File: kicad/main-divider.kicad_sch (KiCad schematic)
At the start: 28 parts, among them U11 TL074, U12 CD4024

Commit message: component positioning mostly done
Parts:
- C46, C47, C48: footprint rumblesan-standard-parts:C_Rect_L7.0mm_W3.5mm_P5.00mm -> rumblesan-standard-parts:C_Rect_L7.0mm_W2.5mm_P5.00mm
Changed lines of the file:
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@@
       (effects (font (size 1.27 1.27)) (justify left))
     )
-    (property "Footprint" "rumblesan-standard-parts:C_Rect_L7.0mm_W3.5mm_P5.00mm" (id 2) (at 248.285 44.45 90)
+    (property "Footprint" "rumblesan-standard-parts:C_Rect_L7.0mm_W2.5mm_P5.00mm" (id 2) (at 248.285 44.45 90)
       (effects (font (size 1.27 1.27)) hide)
     )
@@
       (effects (font (size 1.27 1.27)) (justify left))
     )
-    (property "Footprint" "rumblesan-standard-parts:C_Rect_L7.0mm_W3.5mm_P5.00mm" (id 2) (at 117.475 49.53 90)
+    (property "Footprint" "rumblesan-standard-parts:C_Rect_L7.0mm_W2.5mm_P5.00mm" (id 2) (at 117.475 49.53 90)
       (effects (font (size 1.27 1.27)) hide)
     )
@@
       (effects (font (size 1.27 1.27)) (justify left))
     )
-    (property "Footprint" "rumblesan-standard-parts:C_Rect_L7.0mm_W3.5mm_P5.00mm" (id 2) (at 248.285 57.15 90)
-      (effects (font (size 1.27 1.27)) hide)
-    )
+    (property "Footprint" "rumblesan-standard-parts:C_Rect_L7.0mm_W2.5mm_P5.00mm" (id 2) (at 248.285 57.15 90)
+      (effects (font (size 1.27 1.27)) hide)
+    )

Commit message: initial layout done
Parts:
- removed R65: 47k, rumblesan-standard-parts:R_Axial_DIN0207_L6.3mm_D2.5mm_P10.16mm_Horizontal, symbol rumblesan-standard-parts:R
- C45: footprint rumblesan-standard-parts:C_Rect_L7.0mm_W3.5mm_P5.00mm -> rumblesan-standard-parts:C_Rect_L7.0mm_W2.5mm_P5.00mm
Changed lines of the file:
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@@
   (junction (at 138.43 101.6) (diameter 0) (color 0 0 0 0)
-  )
-  (junction (at 36.83 68.58) (diameter 0) (color 0 0 0 0)
   )
   (junction (at 85.09 68.58) (diameter 0) (color 0 0 0 0)
@@
     (stroke (width 0) (type default) (color 0 0 0 0))
   )
-  (wire (pts (xy 33.02 68.58) (xy 36.83 68.58))
+  (wire (pts (xy 33.02 68.58) (xy 39.37 68.58))
     (stroke (width 0) (type default) (color 0 0 0 0))
   )
@@
     (stroke (width 0) (type default) (color 0 0 0 0))
   )
-  (wire (pts (xy 36.83 68.58) (xy 39.37 68.58))
-    (stroke (width 0) (type default) (color 0 0 0 0))
-  )
   (wire (pts (xy 165.1 83.82) (xy 168.91 83.82))
     (stroke (width 0) (type default) (color 0 0 0 0))
@@
     (stroke (width 0) (type default) (color 0 0 0 0))
   )
-  (wire (pts (xy 36.83 68.58) (xy 36.83 71.12))
-    (stroke (width 0) (type default) (color 0 0 0 0))
-  )
   (wire (pts (xy 168.91 72.39) (xy 156.21 72.39))
     (stroke (width 0) (type default) (color 0 0 0 0))
@@
   )
   (wire (pts (xy 156.21 64.77) (xy 157.48 64.77))
-    (stroke (width 0) (type default) (color 0 0 0 0))
-  )
-  (wire (pts (xy 36.83 78.74) (xy 36.83 81.28))
     (stroke (width 0) (type default) (color 0 0 0 0))
   )
@@
     (pin "2")
   )
-  (symbol (lib_id "power:GND") (at 36.83 81.28 0) (unit 1)
-    (in_bom yes) (on_board yes) (fields_autoplaced)
-    (property "Reference" "#PWR0106" (id 0) (at 36.83 87.63 0)
-      (effects (font (size 1.27 1.27)) hide)
-    )
-    (property "Value" "GND" (id 1) (at 36.83 85.7234 0))
-    (property "Footprint" "" (id 2) (at 36.83 81.28 0)
-      (effects (font (size 1.27 1.27)) hide)
-    )
-    (property "Datasheet" "" (id 3) (at 36.83 81.28 0)
-      (effects (font (size 1.27 1.27)) hide)
-    )
-    (pin "1")
-  )
   (symbol (lib_id "rumblesan-standard-parts:R") (at 161.29 54.61 90) (unit 1)
     (in_bom yes) (on_board yes)
@@
     (property "Reference" "C45" (id 0) (at 54.61 62.7212 90))
     (property "Value" "1nF" (id 1) (at 54.61 65.2581 90))
-    (property "Footprint" "rumblesan-standard-parts:C_Rect_L7.0mm_W3.5mm_P5.00mm" (id 2) (at 53.34 62.865 90)
+    (property "Footprint" "rumblesan-standard-parts:C_Rect_L7.0mm_W2.5mm_P5.00mm" (id 2) (at 53.34 62.865 90)
       (effects (font (size 1.27 1.27)) hide)
     )
@@
     (pin "1")
   )
-  (symbol (lib_id "rumblesan-standard-parts:R") (at 36.83 74.93 0) (unit 1)
-    (in_bom yes) (on_board yes) (fields_autoplaced)
-    (property "Reference" "R65" (id 0) (at 38.608 74.0953 0)
-      (effects (font (size 1.27 1.27)) (justify left))
-    )
-    (property "Value" "47k" (id 1) (at 38.608 76.6322 0)
-      (effects (font (size 1.27 1.27)) (justify left))
-    )
-    (property "Footprint" "rumblesan-standard-parts:R_Axial_DIN0207_L6.3mm_D2.5mm_P10.16mm_Horizontal" (id 2) (at 39.37 77.47 90)
-      (effects (font (size 1.27 1.27)) hide)
-    )
-    (property "Datasheet" "~" (id 3) (at 43.18 74.93 90)
-      (effects (font (size 1.27 1.27)) hide)
-    )
-    (property "Tolerance" "1%" (id 4) (at 41.91 81.28 90)
-      (effects (font (size 1.27 1.27)) hide)
-    )
-    (property "Power" "0.5W" (id 5) (at 41.91 67.31 90)
-      (effects (font (size 1.27 1.27)) hide)
-    )
-    (property "Spec" "metal film" (id 6) (at 41.91 74.93 90)
-      (effects (font (size 1.27 1.27)) hide)
-    )
-    (pin "1")
-    (pin "2")
-  )
   (symbol (lib_id "power:GND") (at 85.09 81.28 0) (unit 1)

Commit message: Final changes for rev01
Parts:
- removed D19: 1n4148, rumblesan-standard-parts:D_DO-35_SOD27_P7.62mm_Horizontal, symbol Device:D
- removed R66, R83: 1k, rumblesan-standard-parts:R_Axial_DIN0207_L6.3mm_D2.5mm_P10.16mm_Horizontal, symbol rumblesan-standard-parts:R
- removed R84: 10k, rumblesan-standard-parts:R_Axial_DIN0207_L6.3mm_D2.5mm_P10.16mm_Horizontal, symbol rumblesan-standard-parts:R
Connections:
- net CLOCK: now also C45.1
- net OUT: now also U11.7, U12.2 (MR)
- net at C45.2: now also R68.1, U11.13 (-)
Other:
- moved on the sheet: C45
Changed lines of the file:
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@@
   (junction (at 233.68 63.5) (diameter 0) (color 0 0 0 0)
-  )
-  (junction (at 208.28 106.68) (diameter 0) (color 0 0 0 0)
   )
   (junction (at 194.31 106.68) (diameter 0) (color 0 0 0 0)
@@
     (stroke (width 0) (type default) (color 0 0 0 0))
   )
-  (wire (pts (xy 208.28 118.11) (xy 208.28 120.65))
-    (stroke (width 0) (type default) (color 0 0 0 0))
-  )
   (wire (pts (xy 85.09 49.53) (xy 91.44 49.53))
     (stroke (width 0) (type default) (color 0 0 0 0))
@@
     (stroke (width 0) (type default) (color 0 0 0 0))
   )
-  (wire (pts (xy 33.02 68.58) (xy 39.37 68.58))
-    (stroke (width 0) (type default) (color 0 0 0 0))
-  )
   (wire (pts (xy 137.16 101.6) (xy 138.43 101.6))
     (stroke (width 0) (type default) (color 0 0 0 0))
   )
-  (wire (pts (xy 194.31 106.68) (xy 196.85 106.68))
+  (wire (pts (xy 194.31 106.68) (xy 199.39 106.68))
     (stroke (width 0) (type default) (color 0 0 0 0))
   )
@@
     (stroke (width 0) (type default) (color 0 0 0 0))
   )
-  (wire (pts (xy 208.28 106.68) (xy 212.09 106.68))
-    (stroke (width 0) (type default) (color 0 0 0 0))
-  )
   (wire (pts (xy 165.1 59.69) (xy 168.91 59.69))
     (stroke (width 0) (type default) (color 0 0 0 0))
   )
-  (wire (pts (xy 58.42 68.58) (xy 62.23 68.58))
+  (wire (pts (xy 80.01 68.58) (xy 85.09 68.58))
     (stroke (width 0) (type default) (color 0 0 0 0))
   )
@@
     (stroke (width 0) (type default) (color 0 0 0 0))
   )
-  (wire (pts (xy 204.47 106.68) (xy 208.28 106.68))
-    (stroke (width 0) (type default) (color 0 0 0 0))
-  )
   (wire (pts (xy 85.09 49.53) (xy 85.09 63.5))
     (stroke (width 0) (type default) (color 0 0 0 0))
   )
-  (wire (pts (xy 69.85 68.58) (xy 85.09 68.58))
-    (stroke (width 0) (type default) (color 0 0 0 0))
-  )
   (wire (pts (xy 156.21 83.82) (xy 157.48 83.82))
     (stroke (width 0) (type default) (color 0 0 0 0))
@@
     (stroke (width 0) (type default) (color 0 0 0 0))
   )
-  (wire (pts (xy 46.99 68.58) (xy 50.8 68.58))
+  (wire (pts (xy 67.31 68.58) (xy 72.39 68.58))
     (stroke (width 0) (type default) (color 0 0 0 0))
   )
@@
   )
   (wire (pts (xy 101.6 69.85) (xy 101.6 124.46))
-    (stroke (width 0) (type default) (color 0 0 0 0))
-  )
-  (wire (pts (xy 208.28 106.68) (xy 208.28 110.49))
     (stroke (width 0) (type default) (color 0 0 0 0))
   )
@@
     (effects (font (size 1.27 1.27)) (justify right))
   )
-  (hierarchical_label "CLOCK" (shape input) (at 33.02 68.58 180)
+  (hierarchical_label "CLOCK" (shape input) (at 67.31 68.58 180)
     (effects (font (size 1.27 1.27)) (justify right))
   )
-  (hierarchical_label "OUT" (shape input) (at 212.09 106.68 0)
+  (hierarchical_label "OUT" (shape input) (at 199.39 106.68 0)
     (effects (font (size 1.27 1.27)) (justify left))
   )
@@
     (pin "1")
   )
-  (symbol (lib_id "rumblesan-standard-parts:C") (at 54.61 68.58 90) (unit 1)
-    (in_bom yes) (on_board yes) (fields_autoplaced)
-    (property "Reference" "C45" (id 0) (at 54.61 62.7212 90))
-    (property "Value" "1nF" (id 1) (at 54.61 65.2581 90))
-    (property "Footprint" "rumblesan-standard-parts:C_Rect_L7.0mm_W2.5mm_P5.00mm" (id 2) (at 53.34 62.865 90)
-      (effects (font (size 1.27 1.27)) hide)
-    )
-    (property "Datasheet" "~" (id 3) (at 54.61 60.96 90)
-      (effects (font (size 1.27 1.27)) hide)
-    )
-    (property "Spec" "ceramic C0G" (id 4) (at 54.61 64.77 90)
-      (effects (font (size 1.27 1.27)) hide)
-    )
-    (property "Tolerance" "5%" (id 5) (at 46.355 64.77 90)
-      (effects (font (size 1.27 1.27)) hide)
-    )
-    (pin "1")
-    (pin "2")
-  )
-  (symbol (lib_id "rumblesan-standard-parts:R") (at 43.18 68.58 90) (unit 1)
-    (in_bom yes) (on_board yes) (fields_autoplaced)
-    (property "Reference" "R66" (id 0) (at 43.18 63.8642 90))
-    (property "Value" "1k" (id 1) (at 43.18 66.4011 90))
-    (property "Footprint" "rumblesan-standard-parts:R_Axial_DIN0207_L6.3mm_D2.5mm_P10.16mm_Horizontal" (id 2) (at 45.72 66.04 90)
-      (effects (font (size 1.27 1.27)) hide)
-    )
-    (property "Datasheet" "~" (id 3) (at 43.18 62.23 90)
-      (effects (font (size 1.27 1.27)) hide)
-    )
-    (property "Tolerance" "1%" (id 4) (at 49.53 63.5 90)
-      (effects (font (size 1.27 1.27)) hide)
-    )
-    (property "Power" "0.5W" (id 5) (at 35.56 63.5 90)
-      (effects (font (size 1.27 1.27)) hide)
-    )
-    (property "Spec" "metal film" (id 6) (at 43.18 63.5 90)
+  (symbol (lib_id "rumblesan-standard-parts:C") (at 76.2 68.58 90) (unit 1)
+    (in_bom yes) (on_board yes) (fields_autoplaced)
+    (property "Reference" "C45" (id 0) (at 76.2 62.7212 90))
+    (property "Value" "1nF" (id 1) (at 76.2 65.2581 90))
+    (property "Footprint" "rumblesan-standard-parts:C_Rect_L7.0mm_W2.5mm_P5.00mm" (id 2) (at 74.93 62.865 90)
+      (effects (font (size 1.27 1.27)) hide)
+    )
+    (property "Datasheet" "~" (id 3) (at 76.2 60.96 90)
+      (effects (font (size 1.27 1.27)) hide)
+    )
+    (property "Spec" "ceramic C0G" (id 4) (at 76.2 64.77 90)
+      (effects (font (size 1.27 1.27)) hide)
+    )
+    (property "Tolerance" "5%" (id 5) (at 67.945 64.77 90)
       (effects (font (size 1.27 1.27)) hide)
     )
@@
     (pin "2")
   )
-  (symbol (lib_id "rumblesan-standard-parts:R") (at 208.28 114.3 0) (unit 1)
-    (in_bom yes) (on_board yes) (fields_autoplaced)
-    (property "Reference" "R84" (id 0) (at 210.058 113.4653 0)
-      (effects (font (size 1.27 1.27)) (justify left))
-    )
-    (property "Value" "10k" (id 1) (at 210.058 116.0022 0)
-      (effects (font (size 1.27 1.27)) (justify left))
-    )
-    (property "Footprint" "rumblesan-standard-parts:R_Axial_DIN0207_L6.3mm_D2.5mm_P10.16mm_Horizontal" (id 2) (at 210.82 116.84 90)
-      (effects (font (size 1.27 1.27)) hide)
-    )
-    (property "Datasheet" "~" (id 3) (at 214.63 114.3 90)
-      (effects (font (size 1.27 1.27)) hide)
-    )
-    (property "Tolerance" "1%" (id 4) (at 213.36 120.65 90)
-      (effects (font (size 1.27 1.27)) hide)
-    )
-    (property "Power" "0.5W" (id 5) (at 213.36 106.68 90)
-      (effects (font (size 1.27 1.27)) hide)
-    )
-    (property "Spec" "metal film" (id 6) (at 213.36 114.3 90)
-      (effects (font (size 1.27 1.27)) hide)
-    )
-    (pin "1")
-    (pin "2")
-  )
   (symbol (lib_id "power:VCC") (at 124.46 40.64 0) (unit 1)
     (in_bom yes) (on_board yes) (fields_autoplaced)
@@
     )
     (property "Spec" "metal film" (id 6) (at 149.86 54.61 90)
-      (effects (font (size 1.27 1.27)) hide)
-    )
-    (pin "1")
-    (pin "2")
-  )
-  (symbol (lib_id "Device:D") (at 66.04 68.58 180) (unit 1)
-    (in_bom yes) (on_board yes) (fields_autoplaced)
-    (property "Reference" "D19" (id 0) (at 66.04 63.6102 0))
-    (property "Value" "1n4148" (id 1) (at 66.04 66.1471 0))
-    (property "Footprint" "rumblesan-standard-parts:D_DO-35_SOD27_P7.62mm_Horizontal" (id 2) (at 66.04 68.58 0)
-      (effects (font (size 1.27 1.27)) hide)
-    )
-    (property "Datasheet" "~" (id 3) (at 66.04 68.58 0)
       (effects (font (size 1.27 1.27)) hide)
     )
@@
     (pin "2")
   )
-  (symbol (lib_id "power:GND") (at 208.28 120.65 0) (unit 1)
-    (in_bom yes) (on_board yes) (fields_autoplaced)
-    (property "Reference" "#PWR0116" (id 0) (at 208.28 127 0)
-      (effects (font (size 1.27 1.27)) hide)
-    )
-    (property "Value" "GND" (id 1) (at 208.28 125.0934 0))
-    (property "Footprint" "" (id 2) (at 208.28 120.65 0)
-      (effects (font (size 1.27 1.27)) hide)
-    )
-    (property "Datasheet" "" (id 3) (at 208.28 120.65 0)
-      (effects (font (size 1.27 1.27)) hide)
-    )
-    (pin "1")
-  )
   (symbol (lib_id "rumblesan-standard-parts:R") (at 161.29 83.82 270) (unit 1)
     (in_bom yes) (on_board yes)
@@
       (effects (font (size 1.27 1.27)) hide)
     )
-    (pin "1")
-    (pin "2")
-  )
-  (symbol (lib_id "rumblesan-standard-parts:R") (at 200.66 106.68 90) (unit 1)
-    (in_bom yes) (on_board yes) (fields_autoplaced)
-    (property "Reference" "R83" (id 0) (at 200.66 101.9642 90))
-    (property "Value" "1k" (id 1) (at 200.66 104.5011 90))
-    (property "Footprint" "rumblesan-standard-parts:R_Axial_DIN0207_L6.3mm_D2.5mm_P10.16mm_Horizontal" (id 2) (at 203.2 104.14 90)
-      (effects (font (size 1.27 1.27)) hide)
-    )
-    (property "Datasheet" "~" (id 3) (at 200.66 100.33 90)
-      (effects (font (size 1.27 1.27)) hide)
-    )
-    (property "Tolerance" "1%" (id 4) (at 207.01 101.6 90)
-      (effects (font (size 1.27 1.27)) hide)
-    )
-    (property "Power" "0.5W" (id 5) (at 193.04 101.6 90)
-      (effects (font (size 1.27 1.27)) hide)
-    )
-    (property "Spec" "metal film" (id 6) (at 200.66 101.6 90)
-      (effects (font (size 1.27 1.27)) hide)
-    )

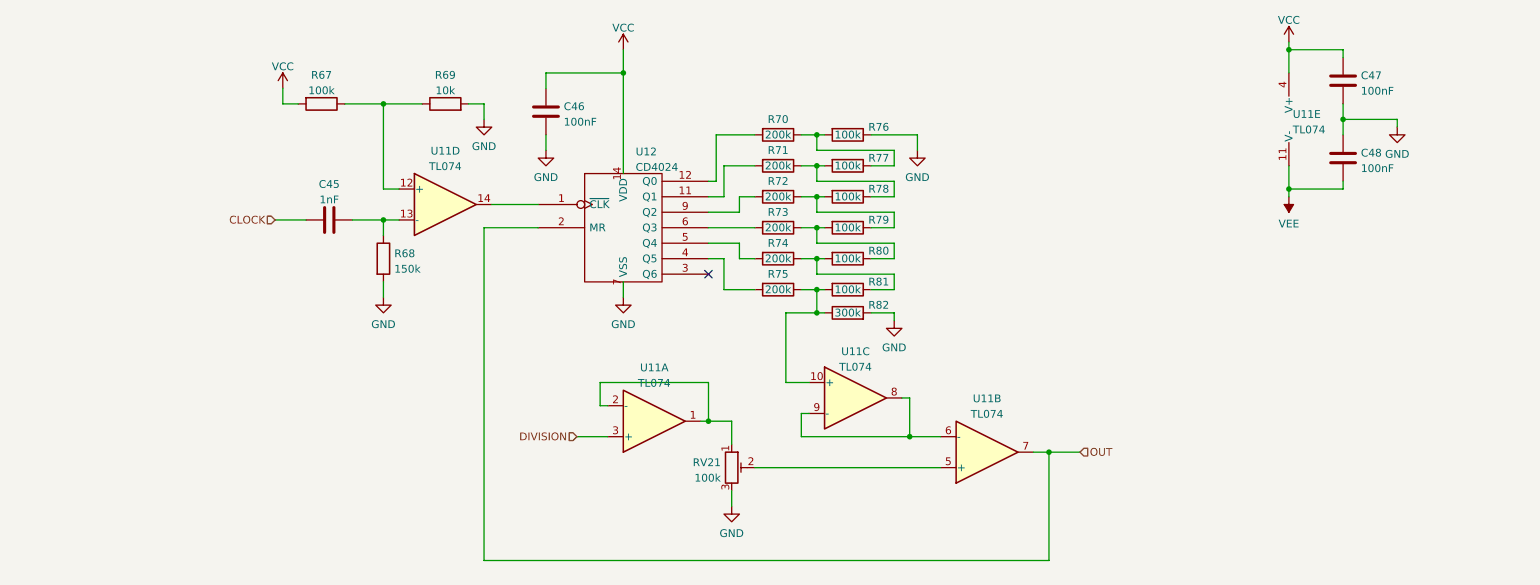
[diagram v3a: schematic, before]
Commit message: Full rejig to use attiny for divider
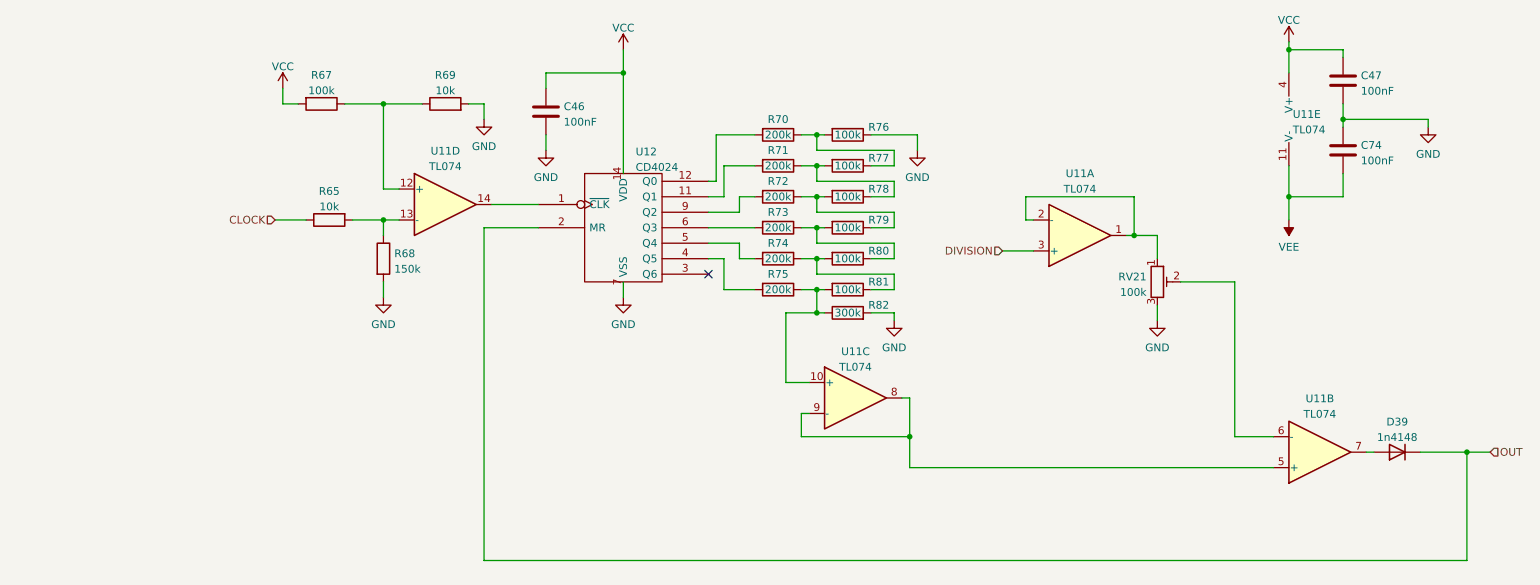
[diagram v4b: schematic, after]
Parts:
- removed C45: 1nF, rumblesan-standard-parts:C_Rect_L7.0mm_W2.5mm_P5.00mm, symbol rumblesan-standard-parts:C
- removed C48: 100nF, rumblesan-standard-parts:C_Rect_L7.0mm_W2.5mm_P5.00mm, symbol rumblesan-standard-parts:C
- added C74: 100nF, rumblesan-standard-parts:C_Rect_L7.0mm_W2.5mm_P5.00mm, symbol rumblesan-standard-parts:C
- added D39: 1n4148, rumblesan-standard-parts:D_DO-35_SOD27_P7.62mm_Horizontal, symbol Device:D
- added R65: 10k, rumblesan-standard-parts:R_Axial_DIN0207_L6.3mm_D2.5mm_P10.16mm_Horizontal, symbol rumblesan-standard-parts:R
- C46, C47: Spec ceramic C0G -> ceramic X7R
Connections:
- net CLOCK: now also R65.1
- net GND: now also C74.1
- net OUT: now also D39.1 (K); no longer U11.7
- net VEE: now also C74.2
- net at R68.1, U11.13 (-): now also R65.2
- net at RV21.2: now also U11.6 (-); no longer U11.5 (+)
- net at U11.8, U11.9 (-): now also U11.5 (+); no longer U11.6 (-)
- new net: D39.2 (A), U11.7
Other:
- moved on the sheet: RV21, U11A, U11B
